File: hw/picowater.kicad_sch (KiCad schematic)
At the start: 10 parts, among them J1 Conn_01x04_MountingPin, J2 Conn_01x02_MountingPin, J3 Conn_01x06_Pin, U1 Pico

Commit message: v0.1
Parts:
- added J4: UART, Connector_PinHeader_2.54mm:PinHeader_1x03_P2.54mm_Vertical, symbol Connector:Conn_01x03_Pin
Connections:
- net GND: now also J3.6 (Pin_6), J4.1 (Pin_1); no longer J3.1 (Pin_1)
- net at U1.14 (GPIO10): now also J3.4 (Pin_4); no longer J3.5 (Pin_5)
- net at U1.15 (GPIO11): now also J3.3 (Pin_3); no longer J3.4 (Pin_4)
- net at U1.16 (GPIO12): now also J3.2 (Pin_2); no longer J3.3 (Pin_3)
- net at U1.21 (GPIO16): now also J4.3 (Pin_3)
- net at U1.22 (GPIO17): now also J4.2 (Pin_2)
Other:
- moved on the sheet: J3
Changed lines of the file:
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@@
     (stroke (width 0) (type default))
   )
-  (wire (pts (xy 107.95 80.01) (xy 123.19 80.01))
+  (wire (pts (xy 170.18 102.87) (xy 180.34 102.87))
+    (stroke (width 0) (type default))
+  )
+  (wire (pts (xy 120.65 81.28) (xy 120.65 95.25))
+    (stroke (width 0) (type default))
+  )
+  (wire (pts (xy 109.22 81.28) (xy 109.22 91.44))
+    (stroke (width 0) (type default))
+  )
+  (wire (pts (xy 49.53 76.2) (xy 82.55 76.2))
+    (stroke (width 0) (type default))
+  )
+  (wire (pts (xy 125.73 90.17) (xy 134.62 90.17))
+    (stroke (width 0) (type default))
+  )
+  (wire (pts (xy 109.22 81.28) (xy 120.65 81.28))
+    (stroke (width 0) (type default))
+  )
+  (wire (pts (xy 82.55 53.34) (xy 106.68 53.34))
+    (stroke (width 0) (type default))
+  )
+  (wire (pts (xy 31.75 76.2) (xy 49.53 76.2))
+    (stroke (width 0) (type default))
+  )
+  (wire (pts (xy 22.86 53.34) (xy 31.75 53.34))
+    (stroke (width 0) (type default))
+  )
+  (wire (pts (xy 22.86 76.2) (xy 31.75 76.2))
+    (stroke (width 0) (type default))
+  )
+  (wire (pts (xy 182.88 105.41) (xy 182.88 114.3))
+    (stroke (width 0) (type default))
+  )
+  (wire (pts (xy 104.14 78.74) (xy 104.14 91.44))
+    (stroke (width 0) (type default))
+  )
+  (wire (pts (xy 106.68 80.01) (xy 106.68 91.44))
+    (stroke (width 0) (type default))
+  )
+  (wire (pts (xy 49.53 53.34) (xy 82.55 53.34))
+    (stroke (width 0) (type default))
+  )
+  (wire (pts (xy 49.53 63.5) (xy 49.53 66.04))
+    (stroke (width 0) (type default))
+  )
+  (wire (pts (xy 22.86 63.5) (xy 22.86 53.34))
+    (stroke (width 0) (type default))
+  )
+  (wire (pts (xy 106.68 53.34) (xy 106.68 40.64))
+    (stroke (width 0) (type default))
+  )
+  (wire (pts (xy 36.83 25.4) (xy 36.83 26.67))
+    (stroke (width 0) (type default))
+  )
+  (wire (pts (xy 36.83 39.37) (xy 36.83 40.64))
+    (stroke (width 0) (type default))
+  )
+  (wire (pts (xy 180.34 102.87) (xy 180.34 114.3))
+    (stroke (width 0) (type default))
+  )
+  (wire (pts (xy 104.14 78.74) (xy 125.73 78.74))
     (stroke (width 0) (type default))
   )
@@
     (stroke (width 0) (type default))
   )
-  (wire (pts (xy 49.53 76.2) (xy 82.55 76.2))
-    (stroke (width 0) (type default))
-  )
-  (wire (pts (xy 125.73 90.17) (xy 134.62 90.17))
-    (stroke (width 0) (type default))
-  )
-  (wire (pts (xy 82.55 53.34) (xy 106.68 53.34))
-    (stroke (width 0) (type default))
-  )
-  (wire (pts (xy 31.75 76.2) (xy 49.53 76.2))
-    (stroke (width 0) (type default))
-  )
-  (wire (pts (xy 22.86 53.34) (xy 31.75 53.34))
-    (stroke (width 0) (type default))
-  )
-  (wire (pts (xy 22.86 76.2) (xy 31.75 76.2))
-    (stroke (width 0) (type default))
-  )
-  (wire (pts (xy 125.73 81.28) (xy 125.73 90.17))
-    (stroke (width 0) (type default))
-  )
-  (wire (pts (xy 49.53 53.34) (xy 82.55 53.34))
-    (stroke (width 0) (type default))
-  )
-  (wire (pts (xy 49.53 63.5) (xy 49.53 66.04))
-    (stroke (width 0) (type default))
-  )
-  (wire (pts (xy 22.86 63.5) (xy 22.86 53.34))
-    (stroke (width 0) (type default))
-  )
-  (wire (pts (xy 106.68 53.34) (xy 106.68 40.64))
-    (stroke (width 0) (type default))
-  )
-  (wire (pts (xy 110.49 81.28) (xy 125.73 81.28))
-    (stroke (width 0) (type default))
-  )
-  (wire (pts (xy 36.83 25.4) (xy 36.83 26.67))
-    (stroke (width 0) (type default))
-  )
-  (wire (pts (xy 36.83 39.37) (xy 36.83 40.64))
-    (stroke (width 0) (type default))
-  )
   (wire (pts (xy 82.55 76.2) (xy 82.55 68.58))
     (stroke (width 0) (type default))
@@
     (stroke (width 0) (type default))
   )
+  (wire (pts (xy 106.68 80.01) (xy 123.19 80.01))
+    (stroke (width 0) (type default))
+  )
   (wire (pts (xy 36.83 40.64) (xy 76.2 40.64))
     (stroke (width 0) (type default))
   )
+  (wire (pts (xy 125.73 78.74) (xy 125.73 90.17))
+    (stroke (width 0) (type default))
+  )
   (wire (pts (xy 49.53 66.04) (xy 55.88 66.04))
     (stroke (width 0) (type default))
@@
     (stroke (width 0) (type default))
   )
-  (wire (pts (xy 105.41 82.55) (xy 105.41 78.74))
-    (stroke (width 0) (type default))
-  )
   (wire (pts (xy 22.86 66.04) (xy 22.86 76.2))
     (stroke (width 0) (type default))
   )
+  (wire (pts (xy 170.18 105.41) (xy 182.88 105.41))
+    (stroke (width 0) (type default))
+  )
   (wire (pts (xy 170.18 59.69) (xy 177.8 59.69))
     (stroke (width 0) (type default))
   )
-  (wire (pts (xy 107.95 82.55) (xy 107.95 80.01))
-    (stroke (width 0) (type default))
-  )
-  (wire (pts (xy 105.41 78.74) (xy 120.65 78.74))
-    (stroke (width 0) (type default))
-  )
   (wire (pts (xy 49.53 53.34) (xy 49.53 55.88))
     (stroke (width 0) (type default))
@@
     (stroke (width 0) (type default))
   )
-  (wire (pts (xy 120.65 78.74) (xy 120.65 95.25))
-    (stroke (width 0) (type default))
-  )
   (wire (pts (xy 120.65 95.25) (xy 134.62 95.25))
     (stroke (width 0) (type default))
   )
-  (wire (pts (xy 110.49 81.28) (xy 110.49 82.55))
-    (stroke (width 0) (type default))
-  )
   (wire (pts (xy 123.19 92.71) (xy 134.62 92.71))
     (stroke (width 0) (type default))
@@
     )
   )
+  (global_label "GND" (shape input) (at 177.8 114.3 90) (fields_autoplaced)
+    (effects (font (size 1.27 1.27)) (justify left))
+    (property "Intersheetrefs" "${INTERSHEET_REFS}" (at 177.8 107.5237 90)
+      (effects (font (size 1.27 1.27)) (justify left) hide)
+    )
+  )
   (global_label "GPIO1" (shape input) (at 109.22 40.64 270) (fields_autoplaced)
     (effects (font (size 1.27 1.27)) (justify right))
@@
     )
   )
+  (global_label "GND" (shape input) (at 99.06 91.44 90) (fields_autoplaced)
+    (effects (font (size 1.27 1.27)) (justify left))
+    (property "Intersheetrefs" "${INTERSHEET_REFS}" (at 99.06 84.6637 90)
+      (effects (font (size 1.27 1.27)) (justify left) hide)
+    )
+  )
   (global_label "GND" (shape input) (at 170.18 62.23 0) (fields_autoplaced)
     (effects (font (size 1.27 1.27)) (justify left))
@@
     (property "Intersheetrefs" "${INTERSHEET_REFS}" (at 126.0294 77.47 0)
       (effects (font (size 1.27 1.27)) (justify right) hide)
-    )
-  )
-  (global_label "GND" (shape input) (at 100.33 82.55 90) (fields_autoplaced)
-    (effects (font (size 1.27 1.27)) (justify left))
-    (property "Intersheetrefs" "${INTERSHEET_REFS}" (at 100.33 75.7737 90)
-      (effects (font (size 1.27 1.27)) (justify left) hide)
     )
   )
@@
         (path "/6f0795e9-9bd6-4197-b73a-51dca38e6e36"
           (reference "#U2") (unit 1)
+        )
+      )
+    )
+  )
+  (symbol (lib_id "Connector:Conn_01x03_Pin") (at 180.34 119.38 90) (unit 1)
+    (in_bom yes) (on_board yes) (dnp no) (fields_autoplaced)
+    (property "Reference" "J4" (at 180.34 121.92 90)
+      (effects (font (size 1.27 1.27)))
+    )
+    (property "Value" "UART" (at 180.34 124.46 90)
+      (effects (font (size 1.27 1.27)))
+    )
+    (property "Footprint" "Connector_PinHeader_2.54mm:PinHeader_1x03_P2.54mm_Vertical" (at 180.34 119.38 0)
+      (effects (font (size 1.27 1.27)) hide)
+    )
+    (property "Datasheet" "~" (at 180.34 119.38 0)
+      (effects (font (size 1.27 1.27)) hide)
+    )
+    (pin "1")
+    (pin "2")
+    (pin "3")
+    (instances
+      (project "picowater"
+        (path "/6f0795e9-9bd6-4197-b73a-51dca38e6e36"
+          (reference "J4") (unit 1)
         )
       )
@@
     )
   )
-  (symbol (lib_id "Connector:Conn_01x06_Pin") (at 105.41 87.63 90) (unit 1)
-    (in_bom yes) (on_board yes) (dnp no) (fields_autoplaced)
-    (property "Reference" "J3" (at 106.68 90.17 90)
-      (effects (font (size 1.27 1.27)))
-    )
-    (property "Value" "Conn_01x06_Pin" (at 106.68 92.71 90)
-      (effects (font (size 1.27 1.27)))
-    )
-    (property "Footprint" "Connector_PinSocket_2.54mm:PinSocket_1x06_P2.54mm_Horizontal" (at 105.41 87.63 0)
-      (effects (font (size 1.27 1.27)) hide)
-    )
-    (property "Datasheet" "~" (at 105.41 87.63 0)
-      (effects (font (size 1.27 1.27)) hide)
-    )
-    (pin "1")
-    (pin "2")
-    (pin "3")
-    (pin "4")
-    (pin "5")
-    (pin "6")
-    (instances
-      (project "picowater"
+  (symbol (lib_id "Connector:Conn_01x06_Pin") (at 106.68 96.52 270) (mirror x) (unit 1)
+    (in_bom yes) (on_board yes) (dnp no) (fields_autoplaced)
+    (property "Reference" "J3" (at 105.41 99.06 90)
+      (effects (font (size 1.27 1.27)))
+    )
+    (property "Value" "Conn_01x06_Pin" (at 105.41 101.6 90)
+      (effects (font (size 1.27 1.27)))
+    )
+    (property "Footprint" "Connector_PinSocket_2.54mm:PinSocket_1x06_P2.54mm_Horizontal" (at 106.68 96.52 0)
+      (effects (font (size 1.27 1.27)) hide)
+    )
+    (property "Datasheet" "~" (at 106.68 96.52 0)
+      (effects (font (size 1.27 1.27)) hide)
+    )
+    (pin "1" (alternate "6"))
+    (pin "2" (alternate "5"))
+    (pin "3" (alternate "4"))
+    (pin "4" (alternate "3"))
+    (pin "5" (alternate "2"))
+    (pin "6" (alternate "1"))
+    (instances
+      (project "picowater"

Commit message: update PCB+code
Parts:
- added D1: 1A 20V Schottky, Diode_SMD:D_SOD-123F, symbol Device:D_Schottky
- added D2: green, LED_THT:LED_D3.0mm, symbol Device:LED
- added H1, H2, H3, H4: MountingHole, MountingHole:MountingHole_2.5mm, symbol Mechanical:MountingHole
- added J5: Power Out, Connector_PinHeader_2.54mm:PinHeader_1x02_P2.54mm_Vertical, symbol Connector_Generic_MountingPin:Conn_01x02_MountingPin
- added R3: 330, Resistor_SMD:R_1206_3216Metric_Pad1.30x1.75mm_HandSolder, symbol Device:R_Small
- J2: value Conn_01x02_MountingPin -> Power In
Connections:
- net +12V: now also J5.2 (Pin_2)
- net +5V: now also D1.2 (A); no longer U1.39 (VSYS)
- net GND: now also U1.33 (AGND), U1.42 (GND), J5.1 (Pin_1), R3.2
- net RX: now reaches J4.2 (Pin_2), U1.22 (GPIO17)
- net TX: now reaches J4.3 (Pin_3), U1.21 (GPIO16)
- net at U1.1 (GPIO0): now also D2.2 (A)
- net at U1.14 (GPIO10): no longer J3.4 (Pin_4)
- net SCL: now reaches J3.3 (Pin_3)
- net SCL: now also U1.17 (GPIO13); no longer U1.15 (GPIO11)
- net SDA: now reaches U1.16 (GPIO12)
- net SDA: now also J3.4 (Pin_4); no longer J3.2 (Pin_2)
- net +3.3V: now reaches U1.36 (3V3)
- net +3.3V: now also J3.5 (Pin_5)
- new net: D1.1 (K), U1.39 (VSYS)
- new net: D2.1 (K), R3.1
- new net SQW: J3.2 (Pin_2), U1.15 (GPIO11)
- no-connect marks 0 -> 17
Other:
- moved on the sheet: J1, R1, R2

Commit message: pcb update
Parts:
- removed J3: Conn_01x06_Pin, Connector_PinSocket_2.54mm:PinSocket_1x06_P2.54mm_Horizontal, symbol Connector:Conn_01x06_Pin
- added J6: RTC, Connector_PinSocket_2.54mm:PinSocket_1x06_P2.54mm_Horizontal, symbol Connector:Conn_01x06_Socket
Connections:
- net GND: now also J6.1 (Pin_1)
- net SCL: now also J6.4 (Pin_4)
- net SDA: now also J6.3 (Pin_3)
- net SQW: now also J6.5 (Pin_5)
- net at U1.14 (GPIO10): now also J6.2 (Pin_2)
- no-connect marks 17 -> 16

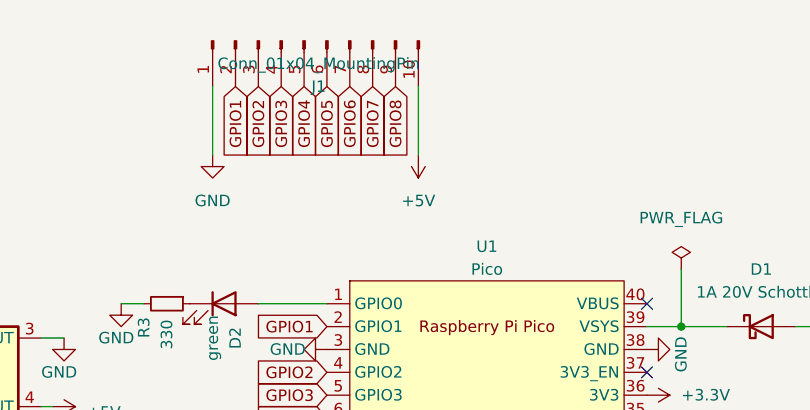
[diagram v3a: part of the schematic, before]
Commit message: use external RTC for wakeup
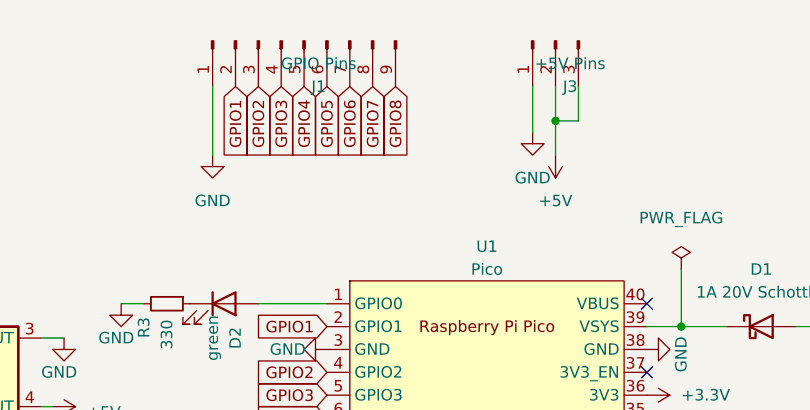
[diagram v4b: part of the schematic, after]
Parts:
- added J3: +5V Pins, Connector_PinHeader_2.54mm:PinHeader_1x03_P2.54mm_Vertical, symbol Connector:Conn_01x03_Pin
- J1: value Conn_01x04_MountingPin -> GPIO Pins; footprint Connector_PinHeader_2.54mm:PinHeader_1x10_P2.54mm_Vertical -> Connector_PinHeader_2.54mm:PinHeader_1x09_P2.54mm_Vertical; symbol Connector:Conn_01x10_Pin -> Connector:Conn_01x09_Pin
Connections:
- net +5V: now also J3.2 (Pin_2), J3.3 (Pin_3); no longer J1.10 (Pin_10)
- net GND: now also J3.1 (Pin_1)
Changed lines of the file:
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@@
   (junction (at 54.61 76.2) (diameter 0) (color 0 0 0 0)
+  )
+  (junction (at 160.02 36.83) (diameter 0) (color 0 0 0 0)
   )
   (no_connect (at 170.18 77.47))
@@
     (stroke (width 0) (type default))
   )
+  (wire (pts (xy 160.02 36.83) (xy 160.02 33.02))
+    (stroke (width 0) (type default))
+  )
+  (wire (pts (xy 160.02 36.83) (xy 162.56 36.83))
+    (stroke (width 0) (type default))
+  )
   (wire (pts (xy 41.91 53.34) (xy 54.61 53.34))
     (stroke (width 0) (type default))
@@
     (stroke (width 0) (type default))
   )
+  (wire (pts (xy 157.48 33.02) (xy 157.48 38.1))
+    (stroke (width 0) (type default))
+  )
   (wire (pts (xy 82.55 76.2) (xy 82.55 68.58))
     (stroke (width 0) (type default))
@@
     (stroke (width 0) (type default))
   )
+  (wire (pts (xy 162.56 33.02) (xy 162.56 36.83))
+    (stroke (width 0) (type default))
+  )
   (wire (pts (xy 41.91 66.04) (xy 41.91 76.2))
     (stroke (width 0) (type default))
@@
     (stroke (width 0) (type default))
   )
-  (wire (pts (xy 144.78 40.64) (xy 144.78 33.02))
+  (wire (pts (xy 160.02 40.64) (xy 160.02 36.83))
     (stroke (width 0) (type default))
   )
@@
     )
   )
+  (symbol (lib_id "power:GND") (at 157.48 38.1 0) (unit 1)
+    (in_bom yes) (on_board yes) (dnp no) (fields_autoplaced)
+    (property "Reference" "#PWR011" (at 157.48 44.45 0)
+      (effects (font (size 1.27 1.27)) hide)
+    )
+    (property "Value" "GND" (at 157.48 43.18 0)
+      (effects (font (size 1.27 1.27)))
+    )
+    (property "Footprint" "" (at 157.48 38.1 0)
+      (effects (font (size 1.27 1.27)) hide)
+    )
+    (property "Datasheet" "" (at 157.48 38.1 0)
+      (effects (font (size 1.27 1.27)) hide)
+    )
+    (pin "1")
+    (instances
+      (project "picowater"
+        (path "/6f0795e9-9bd6-4197-b73a-51dca38e6e36"
+          (reference "#PWR011") (unit 1)
+        )
+      )
+    )
+  )
   (symbol (lib_id "power:+5V") (at 104.14 68.58 270) (unit 1)
     (in_bom yes) (on_board yes) (dnp no) (fields_autoplaced)
@@
     )
   )
+  (symbol (lib_id "Connector:Conn_01x03_Pin") (at 160.02 27.94 90) (mirror x) (unit 1)
+    (in_bom yes) (on_board yes) (dnp no)
+    (property "Reference" "J3" (at 161.6456 33.02 90)
+      (effects (font (size 1.27 1.27)))
+    )
+    (property "Value" "+5V Pins" (at 161.6456 30.48 90)
+      (effects (font (size 1.27 1.27)))
+    )
+    (property "Footprint" "Connector_PinHeader_2.54mm:PinHeader_1x03_P2.54mm_Vertical" (at 160.02 27.94 0)
+      (effects (font (size 1.27 1.27)) hide)
+    )
+    (property "Datasheet" "~" (at 160.02 27.94 0)
+      (effects (font (size 1.27 1.27)) hide)
+    )
+    (pin "1")
+    (pin "2")
+    (pin "3")
+    (instances
+      (project "picowater"
+        (path "/6f0795e9-9bd6-4197-b73a-51dca38e6e36"
+          (reference "J3") (unit 1)
+        )
+      )
+    )
+  )
   (symbol (lib_id "Mechanical:MountingHole") (at 92.71 120.65 0) (unit 1)
     (in_bom yes) (on_board yes) (dnp no) (fields_autoplaced)
@@
     )
   )
-  (symbol (lib_id "power:+5V") (at 144.78 40.64 180) (unit 1)
-    (in_bom yes) (on_board yes) (dnp no) (fields_autoplaced)
-    (property "Reference" "#PWR04" (at 144.78 36.83 0)
-      (effects (font (size 1.27 1.27)) hide)
-    )
-    (property "Value" "+5V" (at 144.78 45.72 0)
-      (effects (font (size 1.27 1.27)))
-    )
-    (property "Footprint" "" (at 144.78 40.64 0)
-      (effects (font (size 1.27 1.27)) hide)
-    )
-    (property "Datasheet" "" (at 144.78 40.64 0)
+  (symbol (lib_id "power:+5V") (at 160.02 40.64 180) (unit 1)
+    (in_bom yes) (on_board yes) (dnp no) (fields_autoplaced)
+    (property "Reference" "#PWR04" (at 160.02 36.83 0)
+      (effects (font (size 1.27 1.27)) hide)
+    )
+    (property "Value" "+5V" (at 160.02 45.72 0)
+      (effects (font (size 1.27 1.27)))
+    )
+    (property "Footprint" "" (at 160.02 40.64 0)
+      (effects (font (size 1.27 1.27)) hide)
+    )
+    (property "Datasheet" "" (at 160.02 40.64 0)
       (effects (font (size 1.27 1.27)) hide)
     )
@@
     )
   )
-  (symbol (lib_id "Connector:Conn_01x10_Pin") (at 132.08 27.94 90) (mirror x) (unit 1)
+  (symbol (lib_id "Connector:Conn_01x09_Pin") (at 132.08 27.94 90) (mirror x) (unit 1)
     (in_bom yes) (on_board yes) (dnp no)
     (property "Reference" "J1" (at 133.7056 33.02 90)
       (effects (font (size 1.27 1.27)))
     )
-    (property "Value" "Conn_01x04_MountingPin" (at 133.7056 30.48 90)
-      (effects (font (size 1.27 1.27)))
-    )
-    (property "Footprint" "Connector_PinHeader_2.54mm:PinHeader_1x10_P2.54mm_Vertical" (at 132.08 27.94 0)
+    (property "Value" "GPIO Pins" (at 133.7056 30.48 90)
+      (effects (font (size 1.27 1.27)))
+    )
+    (property "Footprint" "Connector_PinHeader_2.54mm:PinHeader_1x09_P2.54mm_Vertical" (at 132.08 27.94 0)
       (effects (font (size 1.27 1.27)) hide)
     )
@@
     )
     (pin "1")
-    (pin "10")
     (pin "2")
     (pin "3")
